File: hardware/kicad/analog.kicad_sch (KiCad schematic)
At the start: 12 parts, among them J501 TEMT6000 (modulo)

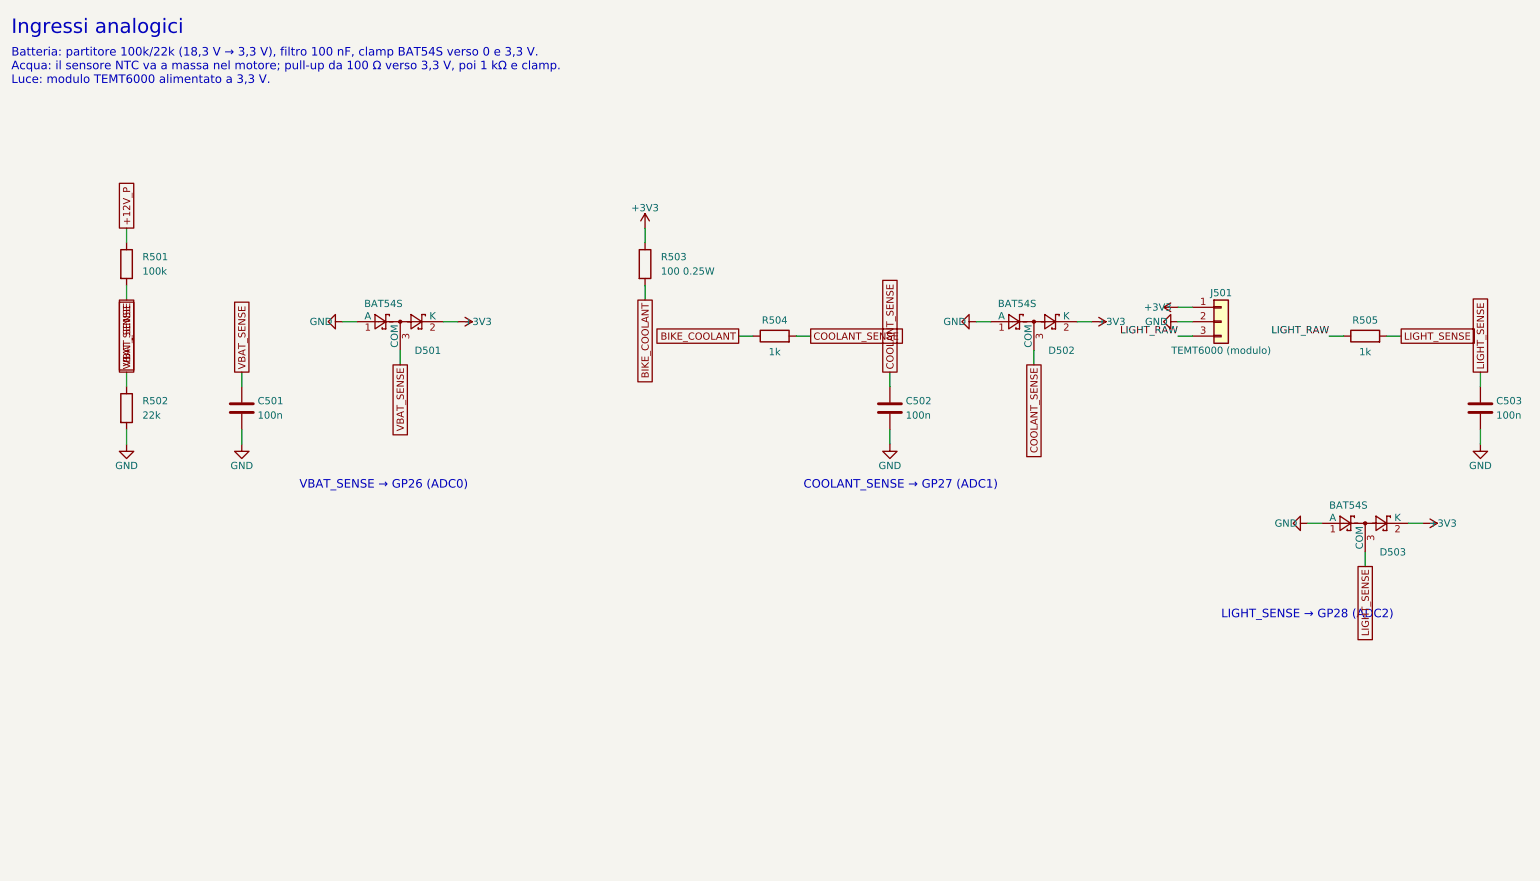
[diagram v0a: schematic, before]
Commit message: Translate code, hardware and docs to English; bilingual dashboard
- tdm-logic i18n module: every dashboard text in English and Italian,
  chosen by `[display] language` in the profile (English by default, the
  TDM 850 profile keeps Italian); number formatting per language
- Slint fixed labels moved to a `Labels` global filled from the same table;
  `tdm-dash --language en|it`; reference screens regenerated in English with
  Italian check screens
- tdmctl, tdm-dash CLI, simulator scenarios, calibration errors and tools
  print English
- KiCad sheets, WireViz harnesses, perfboard plan and CAD comments in
  English, exports regenerated with the new names
- manual, research, ADRs and READMEs translated; files renamed (docs/manual,
  docs/research, English chapter and ADR names); status markers are now
  [VERIFIED] / [TO VERIFY] / [HYPOTHESIS]

Co-Authored-By: Claude Opus 5.5 <noreply@anthropic.com>
Claude-Session: https://claude.ai/code/session_01G9D4Wshjz9MkaThp4wsrGP
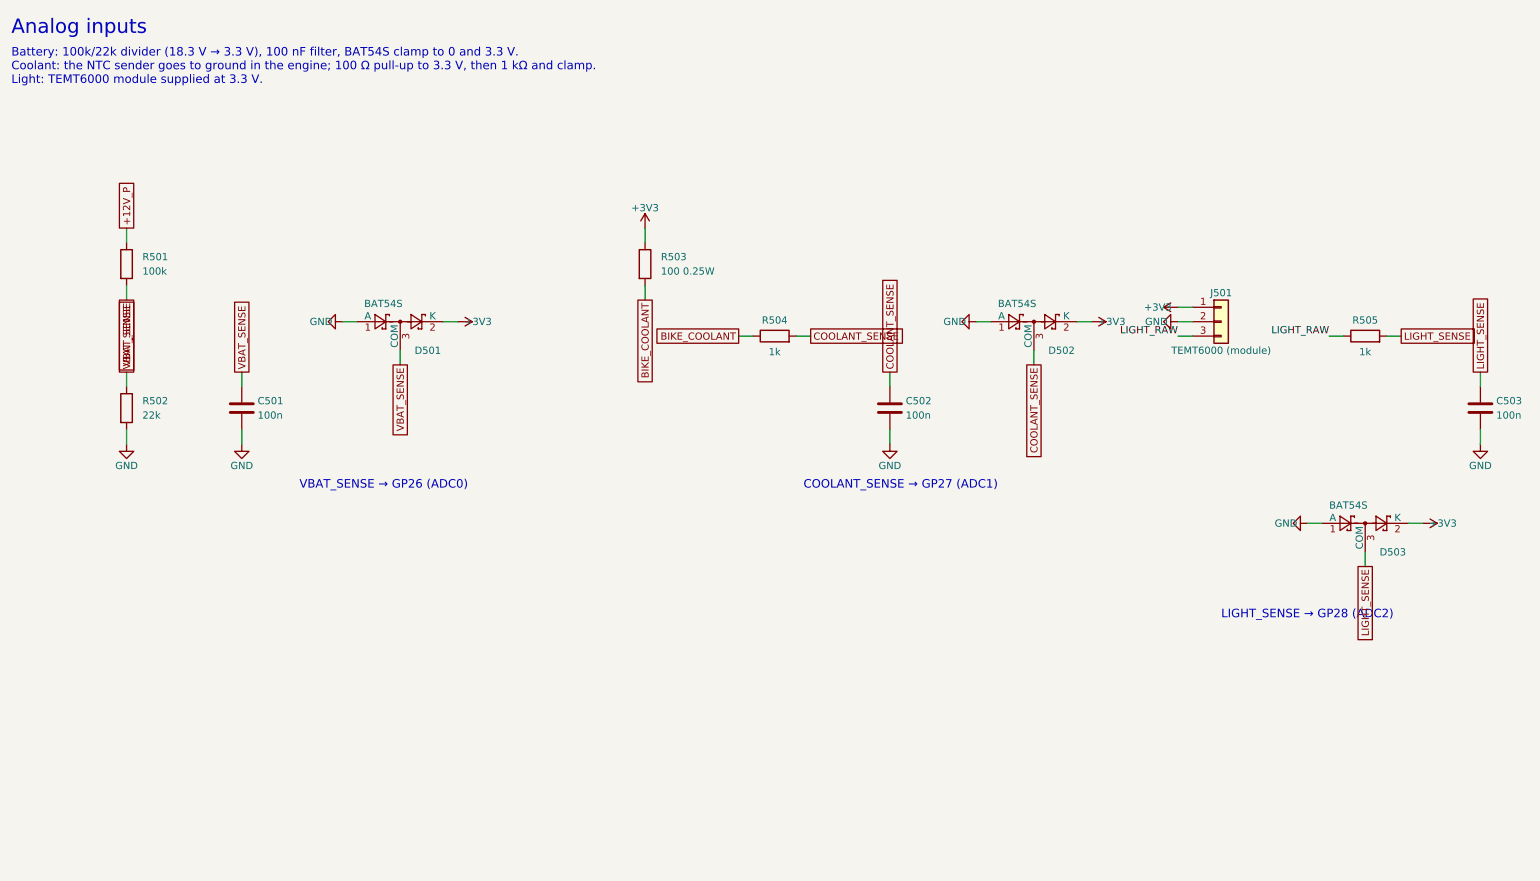
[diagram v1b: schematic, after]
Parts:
- J501: value TEMT6000 (modulo) -> TEMT6000 (module)
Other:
- note added: "Analog inputs"
- note added: "Battery: 100k/22k divider (18.3 V → 3.3 V), 100 nF filter, BAT54S clamp to 0 and 3.3 V. Coolant: the NTC sender goes to ground in the engine; 100 Ω pull-up to 3.3 V, then 1 kΩ and clamp. Light: TEMT6000 module supplied at 3.3 V."
- note removed: "Batteria: partitore 100k/22k (18,3 V → 3,3 V), filtro 100 nF, clamp BAT54S verso 0 e 3,3 V. Acqua: il sensore NTC va a massa nel motore; pull-up da 100 Ω verso 3,3 V, poi 1 kΩ e clamp. Luce: modulo TEMT6000 alimentato a 3,3 V."
- note removed: "Ingressi analogici"
- title: Ingressi analogici -> Analog inputs
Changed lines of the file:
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@@
 	(paper "A4")
 	(title_block
-		(title "Ingressi analogici")
+		(title "Analog inputs")
 		(date "2026-10-21")
 		(rev "0.1")
 		(company "tdm-dash · CERN-OHL-P-2.0")
-		(comment 1 "Foglio 5 di 8")
-		(comment 2 "Generato da hardware/kicad/generate.py: non modificare a mano")
+		(comment 1 "Sheet 5 of 8")
+		(comment 2 "Generated by hardware/kicad/generate.py: do not edit by hand")
 	)
 	(symbol
@@
 			)
 		)
-		(property "Value" "TEMT6000 (modulo)"
+		(property "Value" "TEMT6000 (module)"
 			(at 223.52 71.12 0)
 			(effects
@@
 		)
 	)
-	(text "Ingressi analogici"
+	(text "Analog inputs"
 		(exclude_from_sim no)
 		(at 10.16 12.7 0)
@@
 		)
 	)
-	(text "Batteria: partitore 100k/22k (18,3 V → 3,3 V), filtro 100 nF, clamp BAT54S verso 0 e 3,3 V.\nAcqua: il sensore NTC va a massa nel motore; pull-up da 100 Ω verso 3,3 V, poi 1 kΩ e clamp.\nLuce: modulo TEMT6000 alimentato a 3,3 V."
+	(text "Battery: 100k/22k divider (18.3 V → 3.3 V), 100 nF filter, BAT54S clamp to 0 and 3.3 V.\nCoolant: the NTC sender goes to ground in the engine; 100 Ω pull-up to 3.3 V, then 1 kΩ and clamp.\nLight: TEMT6000 module supplied at 3.3 V."
 		(exclude_from_sim no)
 		(at 10.16 17.78 0)

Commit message: Schematic: drawn wires, block diagram, new title block
The sheets were a netlist in disguise: every pin ended in a short stub and
a label, so the circuits had to be pieced together by name, labels
overlapped, two sheets fell off the index page and the title block was
KiCad's default. The generator now draws the schematic:

- hardware/kicad/schgen: placement on the 50 mil grid, orthogonal wires,
  junctions, hierarchical ports, module and connector symbols with named
  pins; the drawing is normalised the way KiCad 9 reads it and checked
  against the declared netlist (no wire may connect anything else)
- hardware/kicad/sheets: one module per sheet, laid out left to right
  from the bike to the Pico; the root sheet is a block diagram whose
  wires are the signals between sheets
- tdm-dash.kicad_wks: frame and title block of the project
- symbols copied from KiCad 9.0.9 (vendor_symbols.py): the generator no
  longer needs KiCad installed
- export.sh: ERC, tools/check_netlist.py (KiCad's netlist is the declared
  one), check_pinmap.py, PDF and SVG on white, tools/check_svg_layout.py
  (no text over another text, a wire, the frame or the title block)

The circuit is unchanged: KiCad's netlist of the old and new schematic
has the same 56 nets (FRAM pins now follow the breakout header, R603/R604
pins swapped).

Co-Authored-By: Claude Opus 5.5 <noreply@anthropic.com>
Claude-Session: https://claude.ai/code/session_01G9D4Wshjz9MkaThp4wsrGP
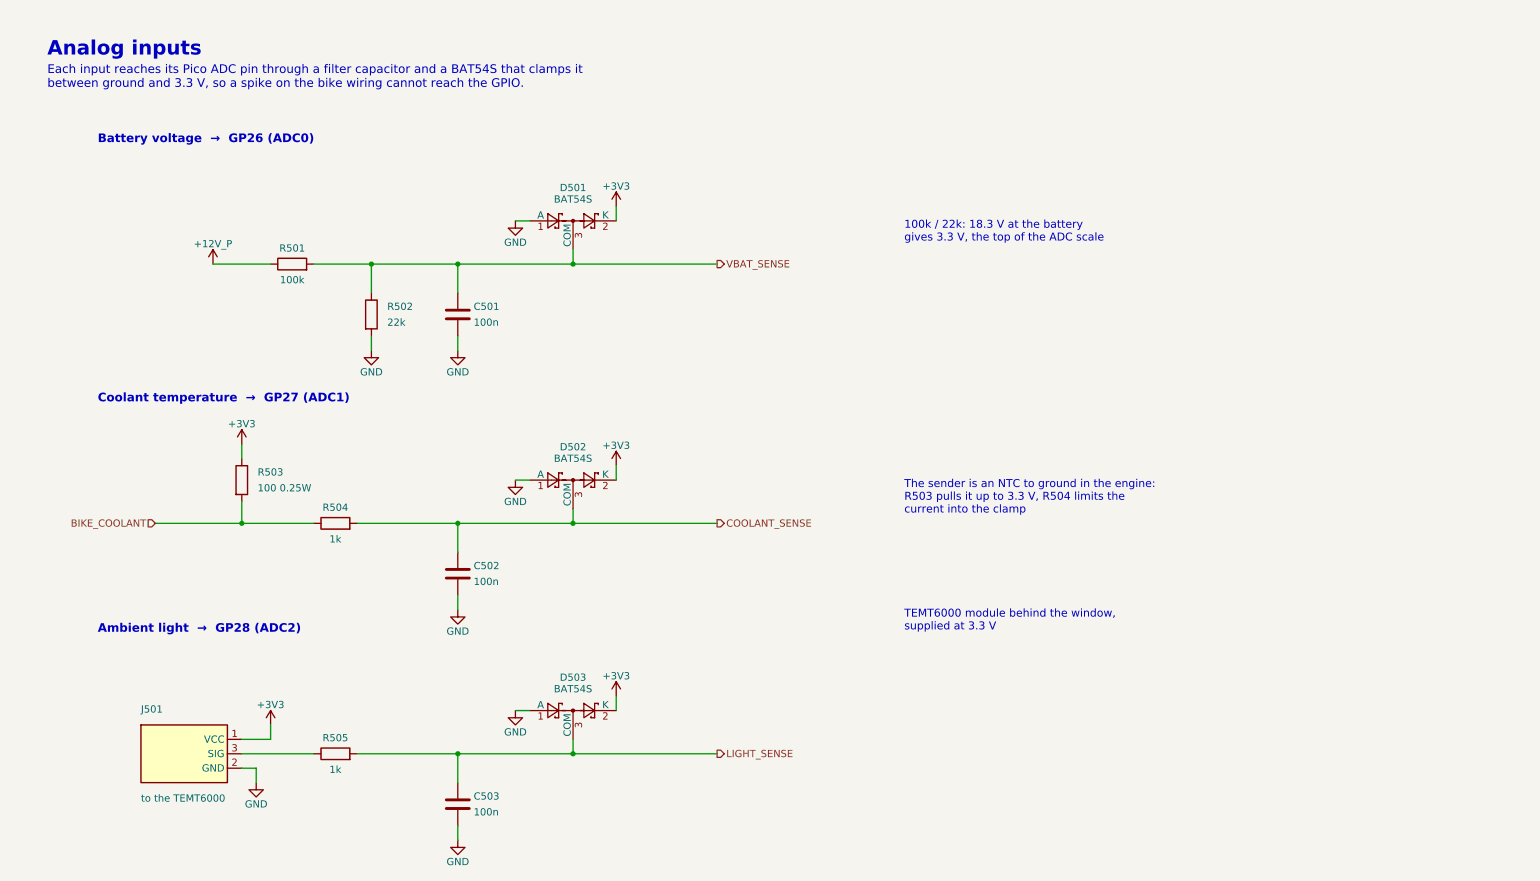
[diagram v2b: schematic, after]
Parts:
- removed J501: TEMT6000 (module), symbol Connector_Generic:Conn_01x03
- added J501: to the TEMT6000, symbol tdm:Conn_Light3
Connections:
- net +3V3: now also J501.1 (VCC)
- net GND: now also J501.2 (GND)
- net LIGHT_RAW: no longer names the net of R505.1
- net LIGHT_RAW: now also J501.3 (SIG)
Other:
- note added: "100k / 22k: 18.3 V at the battery gives 3.3 V, the top of the ADC scale"
- note added: "Ambient light → GP28 (ADC2)"
- note added: "Battery voltage → GP26 (ADC0)"
- note added: "Coolant temperature → GP27 (ADC1)"
- note added: "Each input reaches its Pico ADC pin through a filter capacitor and a BAT54S that clamps it between ground and 3.3 V, so a spike on the bike wiring cannot reach the GPIO."
- note added: "TEMT6000 module behind the window, supplied at 3.3 V"
- note added: "The sender is an NTC to ground in the engine: R503 pulls it up to 3.3 V, R504 limits the current into the clamp"
- note removed: "Battery: 100k/22k divider (18.3 V → 3.3 V), 100 nF filter, BAT54S clamp to 0 and 3.3 V. Coolant: the NTC sender goes to ground in the engine; 100 Ω pull-up to 3.3 V, then 1 kΩ and clamp. Light: TEMT6000 module supplied at 3.3 V."
- note removed: "COOLANT_SENSE → GP27 (ADC1)"
- note removed: "LIGHT_SENSE → GP28 (ADC2)"
- note removed: "VBAT_SENSE → GP26 (ADC0)"
- company: tdm-dash · CERN-OHL-P-2.0 -> tdm-dash
